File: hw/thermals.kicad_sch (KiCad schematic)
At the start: 20 parts, among them M801 5V, Q801 Q_NMOS_GDS

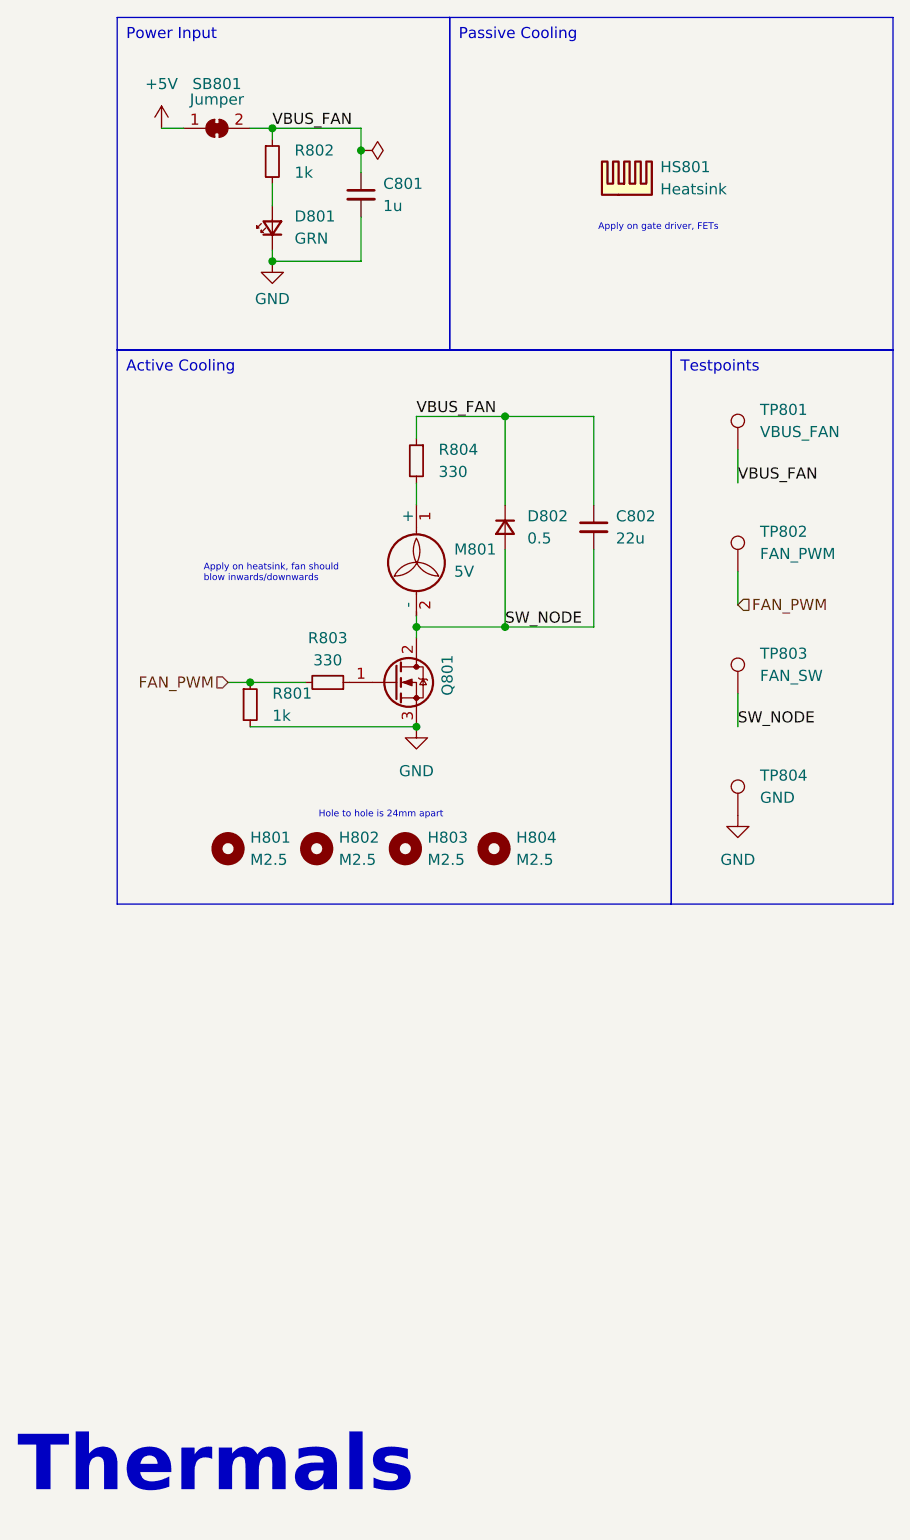
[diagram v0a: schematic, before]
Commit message: HW sch changes, further layout progression
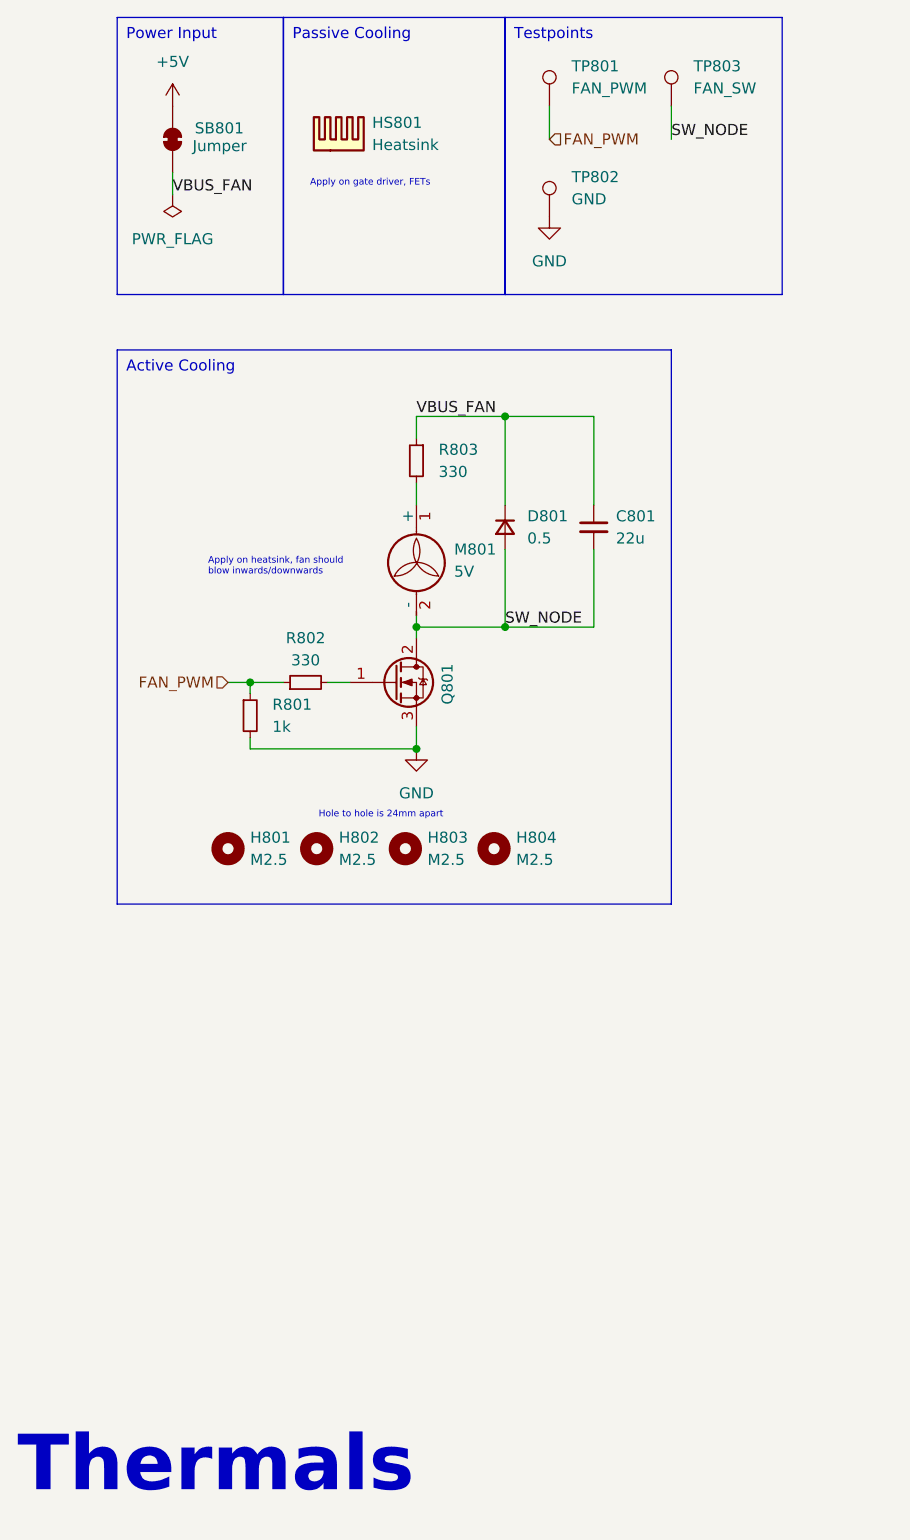
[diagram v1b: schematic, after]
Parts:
- removed C801: 1u, Resistor_SMD:R_0402_1005Metric, symbol Device:C_Small
- removed D801: GRN, LED_SMD:LED_0402_1005Metric, symbol Device:LED_Small
- removed R802: 1k, Resistor_SMD:R_0402_1005Metric, symbol Device:R_Small
- removed TP801: VBUS_FAN, TestPoint:TestPoint_Keystone_5000-5004_Miniature, symbol Connector:TestPoint
- TP801: renamed from TP802; footprint TestPoint:TestPoint_Keystone_5000-5004_Miniature -> TestPoint:TestPoint_Pad_D1.5mm; Cost 0.38 -> (none); Distributor Mouser -> (none); Manufacturer Keystone Electronics -> (none); Notes White (Digital Signal) -> (none); P/N 5002 -> (none)
- TP802: renamed from TP804; footprint TestPoint:TestPoint_Keystone_5000-5004_Miniature -> TestPoint:TestPoint_Pad_D1.5mm; Cost 0.37 -> (none); Distributor Mouser -> (none); Manufacturer Keystone Electronics -> (none); Notes Black (Logic Ground) -> (none); P/N 5001 -> (none)
- TP803: footprint TestPoint:TestPoint_Keystone_5000-5004_Miniature -> TestPoint:TestPoint_Pad_D1.5mm; Cost 0.29 -> (none); Distributor Mouser -> (none); Manufacturer Keystone Electronics -> (none); Notes Green (Analog Signal) -> (none); P/N 5116 -> (none)
- renumbered C802 to C801, D802 to D801, R803 to R802, R804 to R803
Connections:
- net FAN_PWM: now also R802.1; no longer R802.2
- net at Q801.1 (G): now also R802.2; no longer R802.1
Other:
- moved on the sheet: HS801, R801, R802, TP801, TP802, TP803
